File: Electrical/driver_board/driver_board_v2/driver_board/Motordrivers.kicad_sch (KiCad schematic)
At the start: 30 parts, among them J4 Conn_01x04_Socket, J5 Conn_01x04_Socket, J6 Conn_01x04_Socket, J7 Conn_01x04_Socket, J8 Conn_01x04_Socket, J9 Conn_01x04_Socket

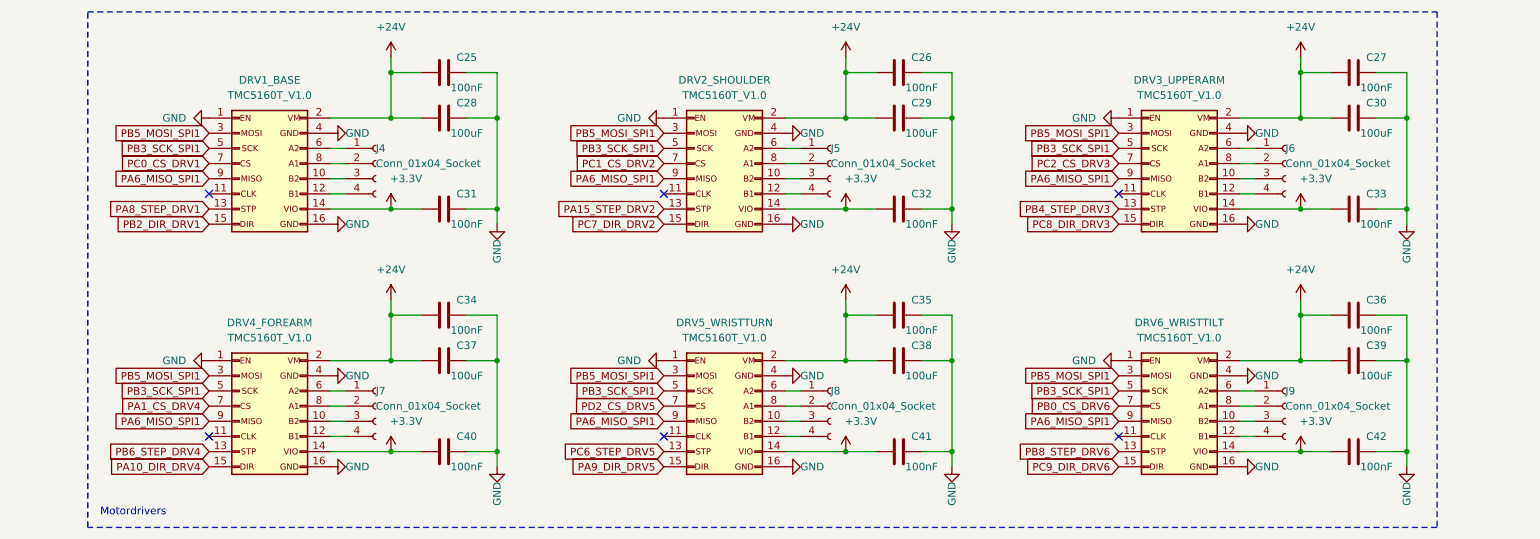
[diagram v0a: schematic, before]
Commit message: Value assignment and protection for driver board
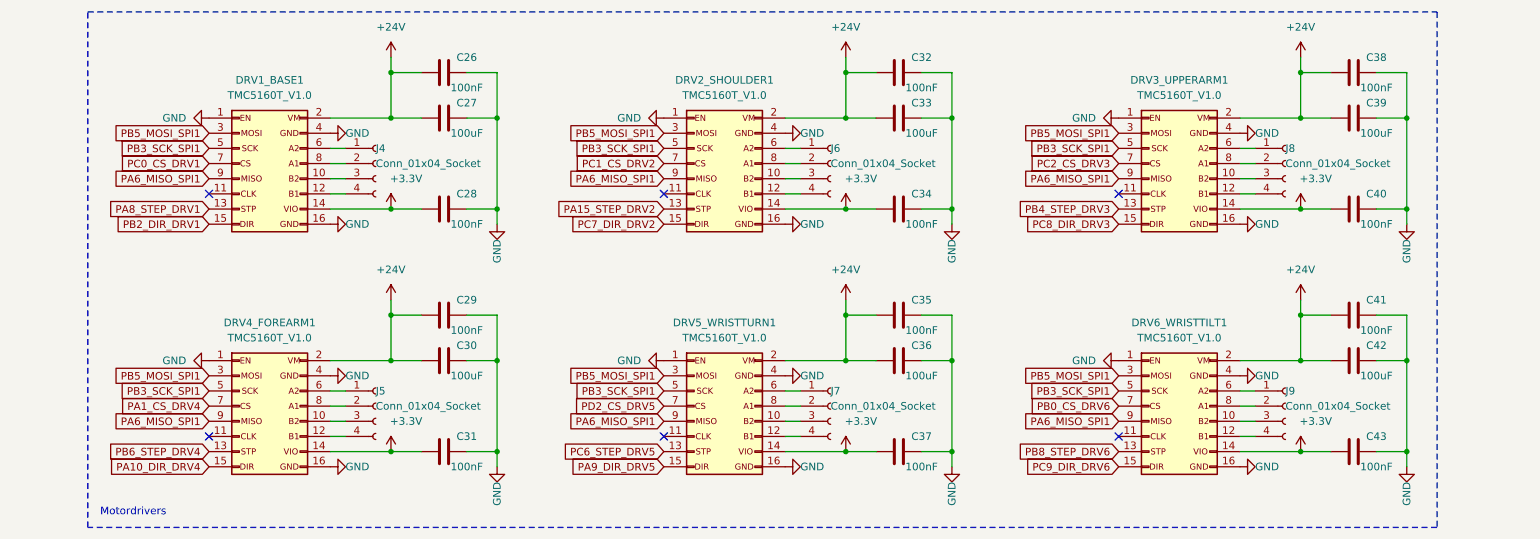
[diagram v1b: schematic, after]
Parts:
- renumbered C25 to C26, C28 to C27, C31 to C28, C34 to C29, C37 to C30, C40 to C31, C26 to C32, C29 to C33, C32 to C34, C38 to C36, C41 to C37, C27 to C38, C30 to C39, C33 to C40, C36 to C41, C39 to C42, C42 to C43, DRV1_BASE to DRV1_BASE1, DRV2_SHOULDER to DRV2_SHOULDER1, DRV3_UPPERARM to DRV3_UPPERARM1, DRV4_FOREARM to DRV4_FOREARM1, DRV5_WRISTTURN to DRV5_WRISTTURN1, DRV6_WRISTTILT to DRV6_WRISTTILT1, J7 to J5, J5 to J6, J8 to J7, J6 to J8

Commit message: Pull up/downs
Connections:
- net GND: now also DRV1_BASE1.11 (Pin_11), DRV2_SHOULDER1.11 (Pin_11), DRV3_UPPERARM1.11 (Pin_11), DRV4_FOREARM1.11 (Pin_11), DRV5_WRISTTURN1.11 (Pin_11), DRV6_WRISTTILT1.11 (Pin_11)
- no-connect marks 6 -> 0

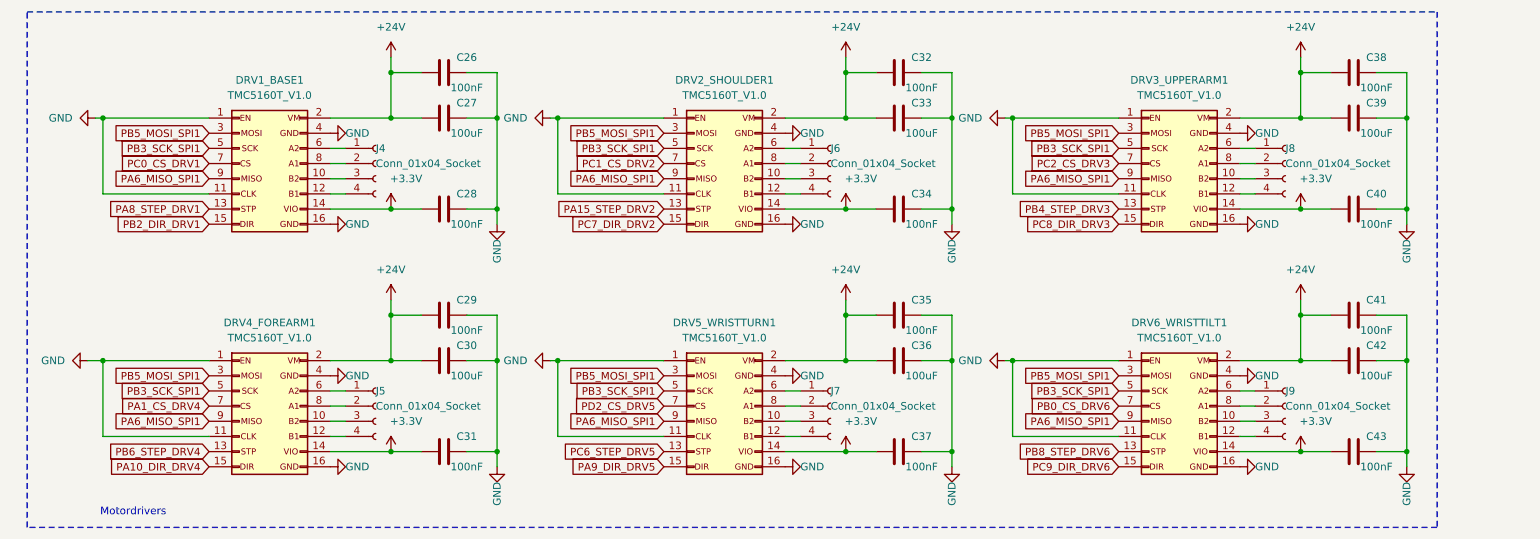
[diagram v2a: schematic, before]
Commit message: Assigned Pull up/downs
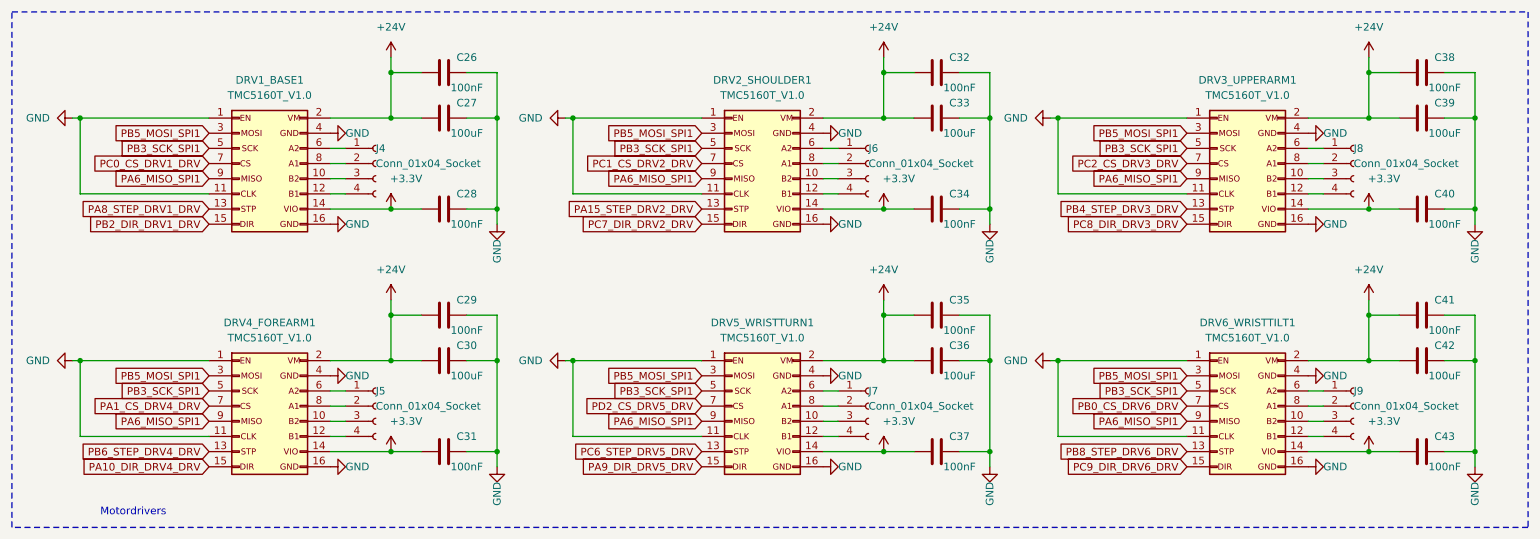
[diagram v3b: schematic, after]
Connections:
- net PA10_DIR_DRV4 renamed PA10_DIR_DRV4_DRV
- net PA15_STEP_DRV2 renamed PA15_STEP_DRV2_DRV
- net PA1_CS_DRV4 renamed PA1_CS_DRV4_DRV
- net PA8_STEP_DRV1 renamed PA8_STEP_DRV1_DRV
- net PA9_DIR_DRV5 renamed PA9_DIR_DRV5_DRV
- net PB0_CS_DRV6 renamed PB0_CS_DRV6_DRV
- net PB2_DIR_DRV1 renamed PB2_DIR_DRV1_DRV
- net PB4_STEP_DRV3 renamed PB4_STEP_DRV3_DRV
- net PB6_STEP_DRV4 renamed PB6_STEP_DRV4_DRV
- net PB8_STEP_DRV6 renamed PB8_STEP_DRV6_DRV
- net PC0_CS_DRV1 renamed PC0_CS_DRV1_DRV
- net PC1_CS_DRV2 renamed PC1_CS_DRV2_DRV
- net PC2_CS_DRV3 renamed PC2_CS_DRV3_DRV
- net PC6_STEP_DRV5 renamed PC6_STEP_DRV5_DRV
- net PC7_DIR_DRV2 renamed PC7_DIR_DRV2_DRV
- net PC8_DIR_DRV3 renamed PC8_DIR_DRV3_DRV
- net PC9_DIR_DRV6 renamed PC9_DIR_DRV6_DRV
- net PD2_CS_DRV5 renamed PD2_CS_DRV5_DRV
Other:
- moved on the sheet: C32, C33, C34, C35, C36, C37, C38, C39, C40, C41, C42, C43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

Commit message: Added new converter
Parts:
- renumbered C26 to C21, C27 to C22, C28 to C23, C29 to C24, C30 to C25, C31 to C26, C32 to C27, C33 to C28, C34 to C29, C35 to C30, C36 to C31, C37 to C32, C38 to C33, C39 to C34, C40 to C35, C41 to C36, C42 to C37, C43 to C38
